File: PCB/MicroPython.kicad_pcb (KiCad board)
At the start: 4 copper layers, 33 x 41.9 mm, 61 parts, among them J1 Conn_01x08, J10 USB4105-GF-A, J2 Conn_01x08, J6 Conn_01x08, J7 Conn_01x08, J8 Conn_02x03_Odd_Even, J9 Conn_01x02, Q1 DMP2160UW, SW1 SW_MEC_5E, SW2 SW_MEC_5E, U1 STM32F405RGT6, U2 MCP1700T, U3 MIC2005A-1YM5, Y1 12 MHz, Y2 32.768 kHz

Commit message: MicroPython v.1.0
MicroPython v.1.0
- DRC=0
- em falta alguns novos OEPSPN
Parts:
- C21, C22, C7, C8: value 12p -> 12pF
- D1: value MSE1PB-M3/89A -> BAS316-TP; footprint Diode_SMD:D_SOD-123 -> Diode_SMD:D_SOD-323
- FB1: value 1k -> 1k@100MHz; footprint Inductor_SMD:L_0603_1608Metric -> Inductor_SMD:L_0402_1005Metric
- J9: footprint Connector_PinHeader_1.00mm:PinHeader_1x02_P1.00mm_Vertical -> Connector_PinHeader_2.54mm:PinHeader_1x02_P2.54mm_Vertical
- Q1: value DMP2160UW -> PMF170XP
- R9: value 220R -> 270R
- SW1, SW2: value SW_MEC_5E -> SW_SPST; footprint Button_Switch_SMD:SW_Push_1P1T_NO_CK_KMR2 -> Button_Switch_SMD:SW_SPST_TL3305B
- moved C6 13.6 mm to (132.6, 71.4), turned to 180 degrees
- moved R21 13.3 mm to (134.7, 71.4)
- moved SW1 5.06 mm to (133.6, 65.8), turned to -90 degrees
- moved C1 2.41 mm to (150.2, 89.5)
- moved U2 2.41 mm to (153.3, 89.4)
- moved SW2 1.90 mm to (133.6, 56.0), turned to -90 degrees
- moved J9 0.92 mm to (144.9, 89.4)
- moved R16 0.81 mm to (137.2, 53.0), turned to 90 degrees
- moved R10 0.18 mm to (133.7, 73.0)
- renumbered Y1 to X1, Y2 to X2
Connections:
- net Net-(U1-PC15-OSC32_OUT) renamed /N2
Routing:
- net GND: track 49.5 -> 22.0 mm, vias 43 -> 63
- net +3V3: track 133.5 -> 126.1 mm
- net /USR-SW: track 5.85 -> 9.73 mm
- net /RST-SW: track 70.6 -> 72.6 mm
- net VBUS: track 58.4 -> 57.4 mm
- net VBAT: track 2.89 -> 3.67 mm
- net /PC5-X12: track 24.1 -> 23.4 mm
- net V+: track 74.9 -> 75.4 mm
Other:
- board text added: "MicroPython v.1.0"

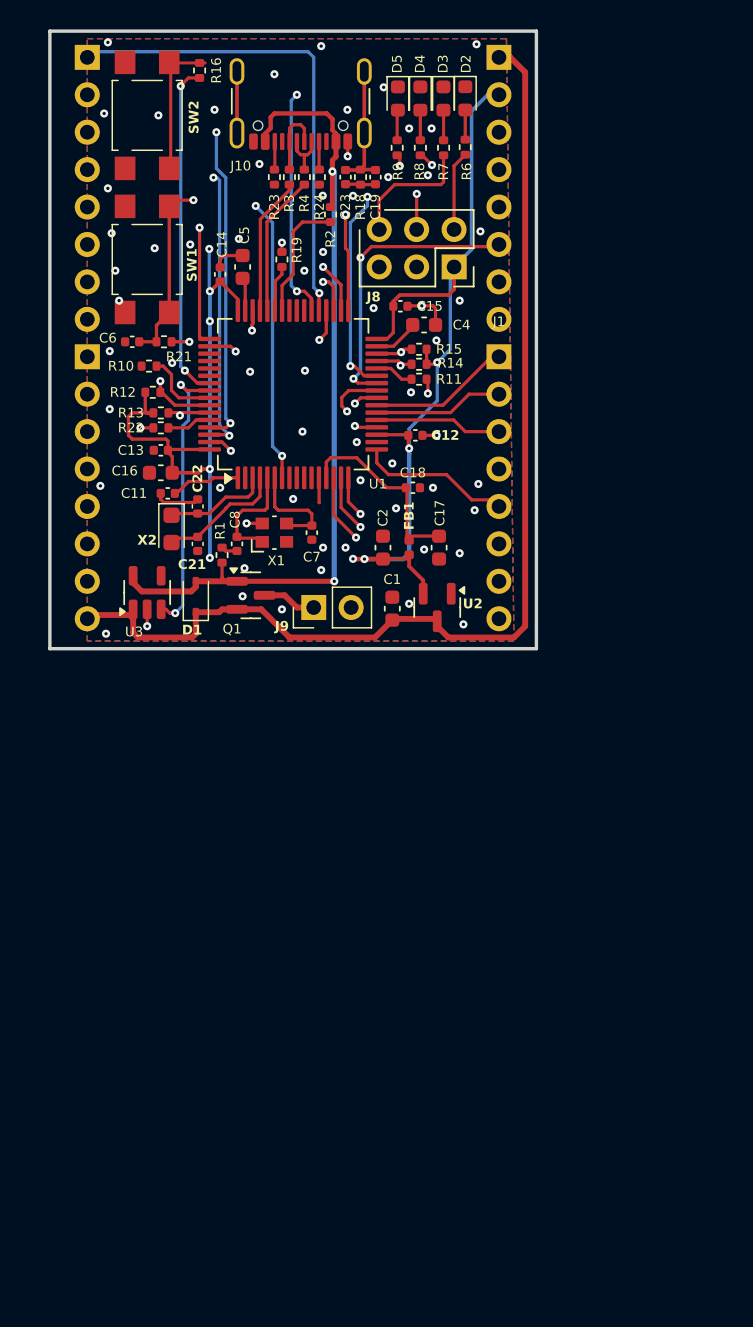
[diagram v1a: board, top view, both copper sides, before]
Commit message: MicroPhython v.1.0
- maior alterações a nivel do rail de PowerIn
- retirado a andar de PFET - em versões anteriores e posteriores à PCB v.1.1 estes andares não exixtiam
- realocação & re-routing na PCB do andar de PowerIn
- DRC=0
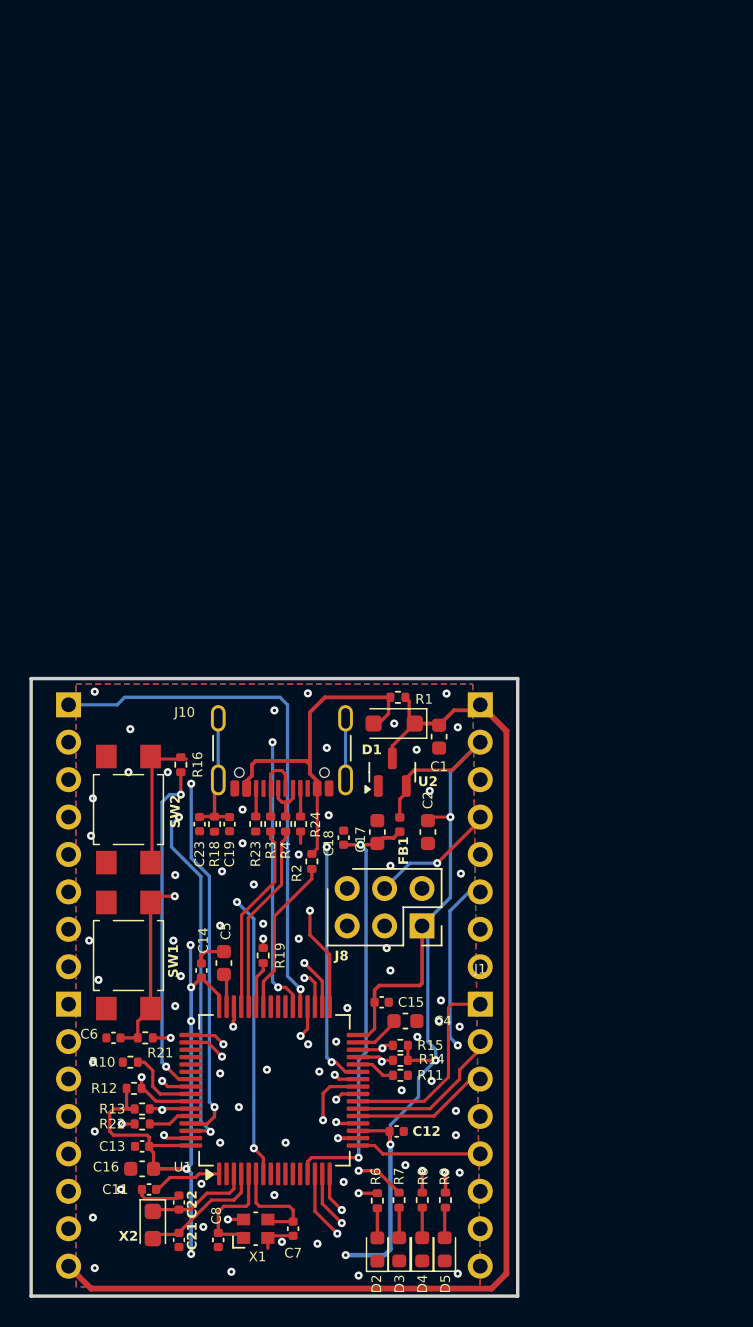
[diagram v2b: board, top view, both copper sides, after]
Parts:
- removed J9: Conn_01x02, Connector_PinHeader_2.54mm:PinHeader_1x02_P2.54mm_Vertical
- removed Q1: PMF170XP, Package_TO_SOT_SMD:SOT-23
- removed U3: MIC2005A-1YM5, Package_TO_SOT_SMD:SOT-23-5
- D1: value BAS316-TP -> SM5817PL; footprint Diode_SMD:D_SOD-323 -> Diode_SMD:D_SOD-123F
- R1: value 100k -> 0R
- moved D2 78.4 mm to (149.2, 133.0), turned to 90 degrees
- moved D5 78.2 mm to (153.8, 133.0), turned to 90 degrees
- moved D3 78.2 mm to (150.7, 133.0), turned to 90 degrees
- moved D4 78.1 mm to (152.3, 133.0), turned to 90 degrees
- moved R6 71.8 mm to (149.2, 129.7), turned to -90 degrees
- moved R9 71.5 mm to (153.8, 129.6), turned to -90 degrees
- moved R7 71.5 mm to (150.7, 129.6), turned to -90 degrees
- moved R8 71.4 mm to (152.3, 129.6), turned to -90 degrees
- moved C13 47.3 mm to (133.3, 126.0)
- moved C15 47.3 mm to (149.5, 116.2)
- moved C16 47.3 mm to (133.3, 127.5)
- moved C22 47.3 mm to (135.8, 129.8)
- moved C4 47.3 mm to (151.1, 117.5)
- moved C5 47.3 mm to (138.8, 113.5)
- moved C6 47.3 mm to (131.3, 118.6)
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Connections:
- net /N2 renamed Net-(U1-PC15-OSC32_OUT)
- C1 pad 1: V+ -> VIN
- C11 pad 1: VBackup -> VBAT
- D1 pad 1: V+ -> VIN
- J2 pad 8: V+ -> VIN
- J7 pad 1: V+ -> VIN
- R1 pad 2: GND -> VIN
- U1 pad 1: VBackup -> VBAT
- U2 pad 3: V+ -> VIN
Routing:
- net VIN: track 0.00 -> 79.5 mm
- net V+: track 75.4 -> 0.00 mm
- net VBUS: track 57.4 -> 24.4 mm, vias 2 -> 0
- net /PB4-TRST: track 51.6 -> 28.6 mm, vias 4 -> 3
- net /VDDA: track 12.9 -> 30.1 mm, vias 0 -> 2
- net /PA13-SWDIO: track 28.6 -> 39.0 mm, vias 1 -> 4
- net +3V3: track 126.1 -> 135.4 mm
- net GND: track 22.0 -> 13.6 mm
- net /PA14-SWCLCK: track 29.1 -> 34.8 mm, vias 1 -> 3
- net VBackup: track 4.72 -> 0.00 mm
- net /RST-SW: track 72.6 -> 68.0 mm
- net /PA7-X8: track 9.66 -> 13.8 mm
- net /PB1-Y12: track 23.3 -> 27.4 mm
- net /PB11-Y10: track 11.7 -> 15.5 mm, vias 1 -> 2
- net /PA0-X1: track 18.9 -> 15.3 mm
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
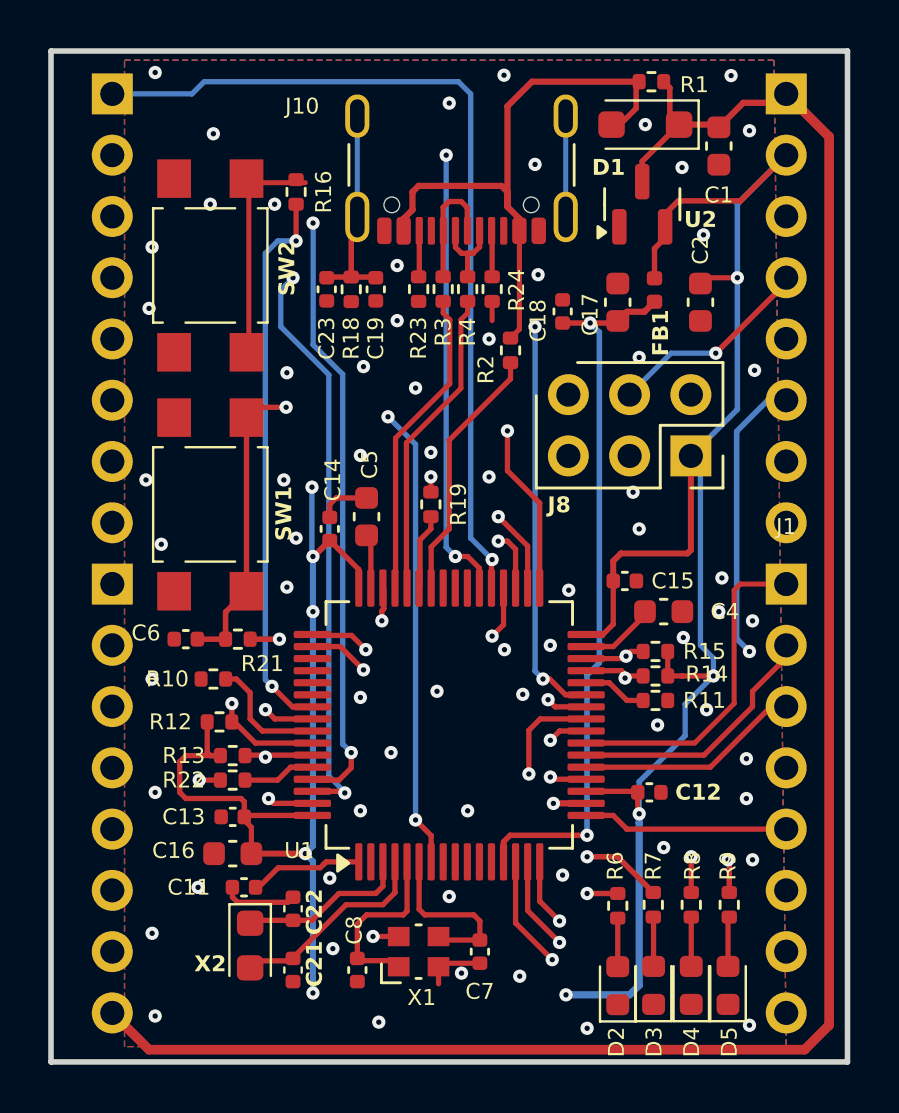
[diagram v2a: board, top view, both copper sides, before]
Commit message: ficheiros de produção gerados
- todos os componentes com OEPS & MPN
- gerados ficheiros de produção \production
- gerada BOM
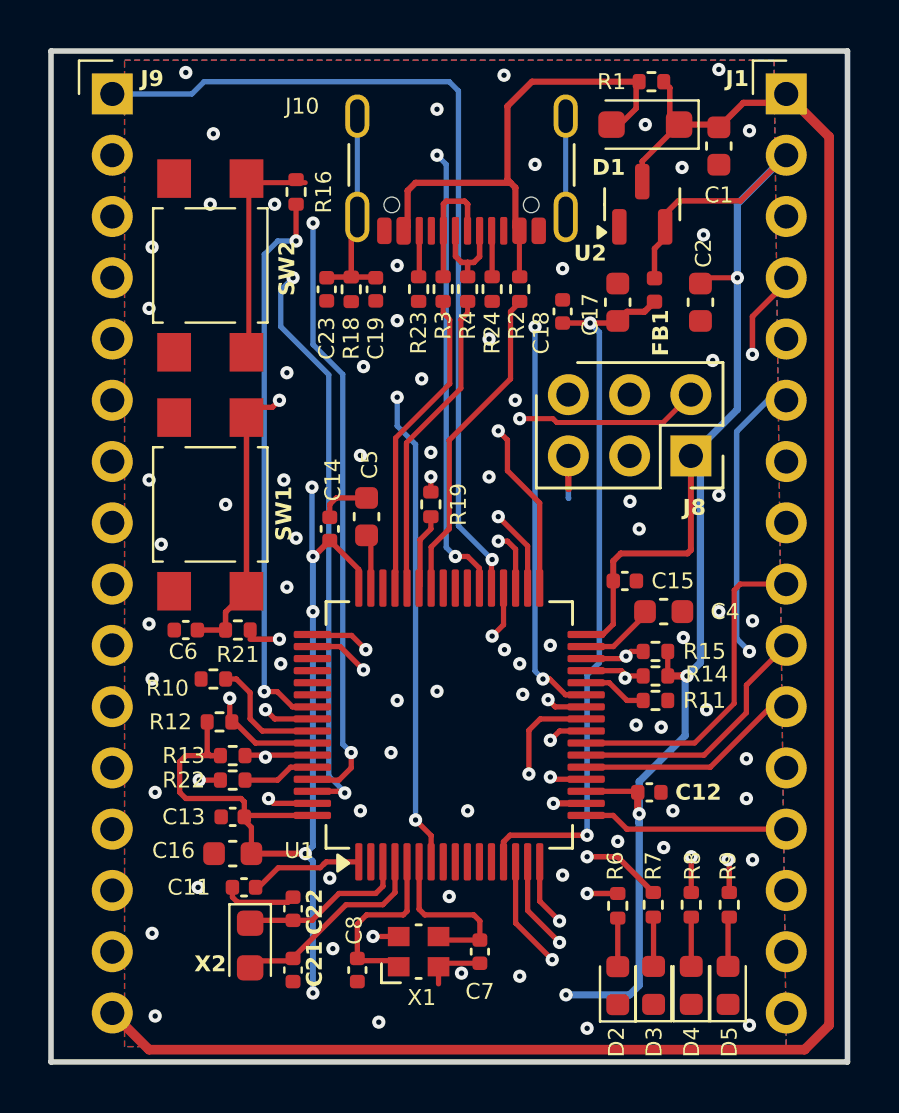
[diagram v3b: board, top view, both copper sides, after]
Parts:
- removed J2, J6, J7: Conn_01x08, Connector_PinHeader_2.54mm:PinHeader_1x08_P2.54mm_Vertical
- added J9: Conn_01x08, Connector_PinHeader_2.54mm:PinHeader_1x16_P2.54mm_Vertical, F.Cu at (128.3, 96.0)
- J1: footprint Connector_PinHeader_2.54mm:PinHeader_1x08_P2.54mm_Vertical -> Connector_PinHeader_2.54mm:PinHeader_1x16_P2.54mm_Vertical
- moved J1 20.3 mm to (156.2, 96.0)
- moved R2 2.57 mm to (145.2, 104.1)
- moved C6 0.38 mm to (131.3, 118.2)
- moved R21 0.38 mm to (133.5, 118.2)
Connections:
- net /PB3-SW-X17 renamed /PB3-SW1
- net Net-(U1-PC15-OSC32_OUT) renamed /N2
- J1 pad 1: /PA7-X8 -> VIN
- J1 pad 2: /PA6-X7 -> +3V3
- J1 pad 3: /PA5-X6 -> GND
- J1 pad 4: /PA4-X5 -> /RST-SW
- J1 pad 5: /PA3-X4 -> /PB1-Y12
- J1 pad 6: /PA2-X3 -> /PB0-Y11
- J1 pad 7: /PA1-X2 -> /PB11-Y10
- J1 pad 8: /PA0-X1 -> /PB10-Y9
- J8 pad 2: /PA13-SWDIO -> /PA14-JTCK
- J8 pad 3: unconnected-(J8-Pin_3-Pad3) -> /PB4-NJTRST
- J8 pad 4: /RST-SW -> /PB6-JTDO
- J8 pad 6: /PA14-SWCLCK -> /PA15-JTDI
- R6 pad 1: /PA13-SWDIO -> /PB6-JTDO
- R7 pad 1: /PA14-SWCLCK -> /PA14-JTCK
- R8 pad 1: /PA15-TDI -> /PA15-JTDI
- R9 pad 1: /PB4-TRST -> /PB4-NJTRST
- U1 pad 46: /PA13-SWDIO -> /PA13-TMS
- U1 pad 49: /PA14-SWCLCK -> /PA14-JTCK
- U1 pad 50: /PA15-TDI -> /PA15-JTDI
- U1 pad 56: /PB4-TRST -> /PB4-NJTRST
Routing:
- net /PB4-NJTRST: track 0.00 -> 40.7 mm, vias 0 -> 4
- net /PA14-JTCK: track 0.00 -> 40.6 mm, vias 0 -> 4
- net /PA15-JTDI: track 0.00 -> 39.4 mm, vias 0 -> 4
- net /PA13-SWDIO: track 39.0 -> 0.00 mm, vias 4 -> 0
- net /PA14-SWCLCK: track 34.8 -> 0.00 mm, vias 3 -> 0
- net /PB4-TRST: track 28.6 -> 0.00 mm, vias 3 -> 0
- net /PA15-TDI: track 27.1 -> 0.00 mm, vias 3 -> 0
- net /PB6-JTDO: track 0.00 -> 23.2 mm, vias 0 -> 1
- net VBUS: track 24.4 -> 21.1 mm
- net /PA9-VBUS: track 10.7 -> 13.4 mm
- net GND: track 13.6 -> 15.9 mm, vias 63 -> 69
- net +3V3: track 135.4 -> 133.8 mm
- net /PB1-Y12: track 27.4 -> 28.0 mm
- net /PB0-Y11: track 23.3 -> 22.8 mm

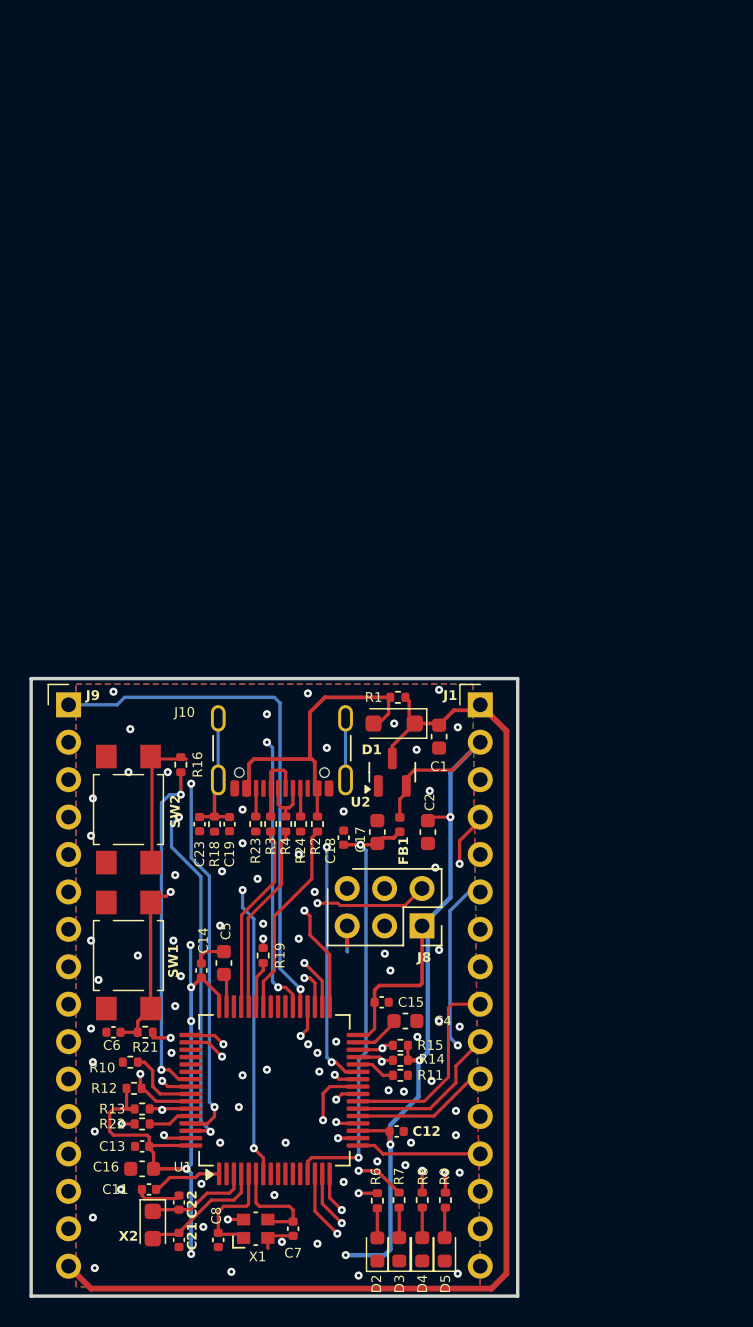
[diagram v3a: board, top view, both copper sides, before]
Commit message: mudanças a partir de mudanças sugeridas pelo Filipe
- projecto commited já com pequenas alterações do Filipe
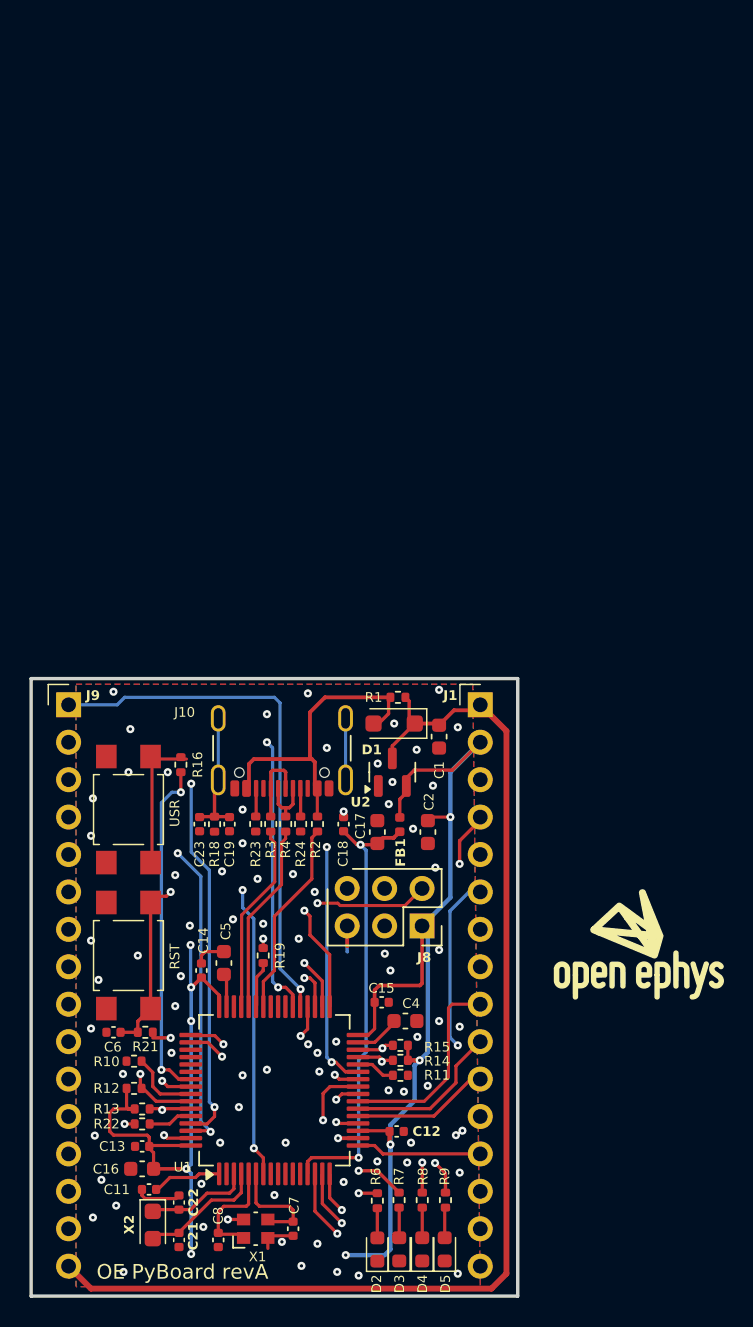
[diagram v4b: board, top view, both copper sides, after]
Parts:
- added G***: LOGO, FED3_PCBLib:oe logo, F.Cu at (167.0, 112.2)
- moved C18 0.92 mm to (146.9, 104.1)
- moved R10 0.26 mm to (132.7, 120.2)
- renumbered SW1 to RST1, SW2 to USR1
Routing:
- net /PB9-Y4: track 31.6 -> 29.6 mm
- net GND: track 15.9 -> 15.7 mm, vias 69 -> 75
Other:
- board text added: "OE PyBoard revA"
- board text added: "RST"
- board text added: "USR"
- board text removed: "MicroPython v.1.0"
